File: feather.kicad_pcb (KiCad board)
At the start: 2 copper layers, 22.9 x 58.6 mm, 24 parts, among them J1 USB_C_Receptacle_USB2.0, J2 Conn_01x04_MountingPin, J3 Conn_ARM_SWD_TagConnect_TC203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, J4 2.54mm Header, J5 Micro_SD_Card_Det_Hirose_DM3AT, J6 2.54mm Header, SW1 BGS12P2L6, U1 TPS22917DBV, U10 TPS22917DBV, U2 nRF5340-CLXX, U3 nPM1100-CAXX, U4 TPS22917DBV, U5 USBLC6-2SC6, U6 TPS62173DSG, U7 MX25R3235FZNxx1, U8 nRF7002-QFXX, U9 TPS22917DBV

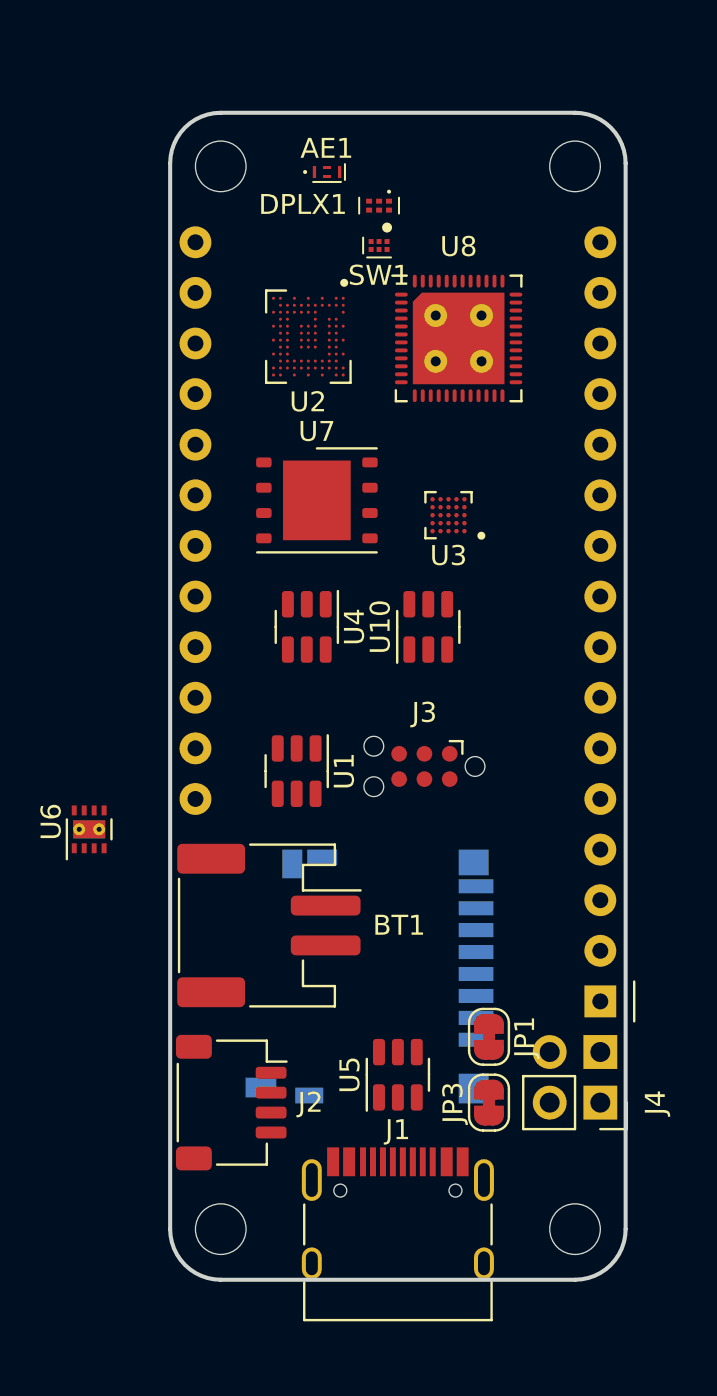
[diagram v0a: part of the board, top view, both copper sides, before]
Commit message: Added passvies and bus connections to nRF7002
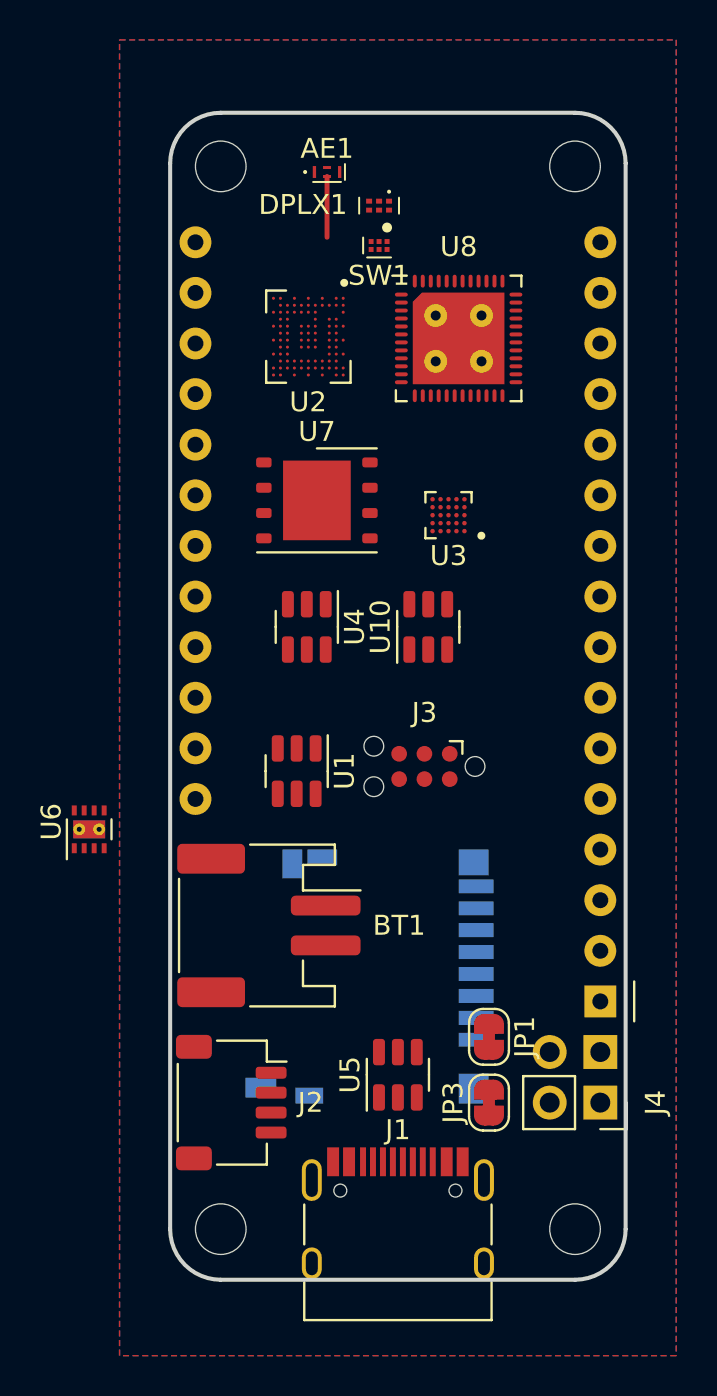
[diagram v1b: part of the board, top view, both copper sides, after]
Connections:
- A1 pad 26: unconnected-(A1-USB-Pad26) -> VBUS
- A1 pad 28: unconnected-(A1-VBAT-Pad28) -> /VBATT_
- U1 pad 1: unconnected-(U1-VIN-Pad1) -> VDD_nRF
- U1 pad 2: unconnected-(U1-GND-Pad2) -> GND
- U1 pad 3: unconnected-(U1-ON-Pad3) -> Net-(U1-ON)
- U1 pad 6: unconnected-(U1-VOUT-Pad6) -> Net-(U1-VOUT)
- U10 pad 1: unconnected-(U10-VIN-Pad1) -> +3.3V
- U10 pad 2: unconnected-(U10-GND-Pad2) -> GND
- U10 pad 3: unconnected-(U10-ON-Pad3) -> Net-(U10-ON)
- U10 pad 6: unconnected-(U10-VOUT-Pad6) -> Net-(U10-VOUT)
- U3 pad D1: /Connectivity/VBAT -> /VBATT_
- U3 pad D2: /Connectivity/VBAT -> /VBATT_
- U4 pad 1: unconnected-(U4-VIN-Pad1) -> +3.3V
- U4 pad 2: unconnected-(U4-GND-Pad2) -> GND
- U4 pad 3: unconnected-(U4-ON-Pad3) -> Net-(U4-ON)
- U4 pad 6: unconnected-(U4-VOUT-Pad6) -> Net-(J5-VDD)
- U7 pad 8: Net-(U7-VCC) -> Net-(U10-VOUT)
- U8 pad 13: /nRF7002/VBATT -> +3.3V
- U8 pad 20: /nRF7002/VBATT -> +3.3V
- U8 pad 31: /nRF7002/VBATT -> +3.3V
- U8 pad 48: unconnected-(U8-IOVDD-Pad48) -> Net-(U1-VOUT)
- U9 pad 1: unconnected-(U9-VIN-Pad1) -> VOUT
- U9 pad 2: unconnected-(U9-GND-Pad2) -> GND
- U9 pad 3: unconnected-(U9-ON-Pad3) -> /PowerSupply/BUCK_EN
- U9 pad 6: unconnected-(U9-VOUT-Pad6) -> Net-(U6-EN)
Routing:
- net Net-(AE1-FEED): track 0.00 -> 3.05 mm
- added copper zone on B.Cu, net GND
- added copper zone on F.Cu, net GND
- added copper zone on In1.Cu, net GND
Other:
- copper layers 2 -> 4

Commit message: Schematic complete.
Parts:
- removed JP2: 400mA Charge, Jumper:SolderJumper-2_P1.3mm_Open_RoundedPad1.0x1.5mm
- removed U1, U10, U9: TPS22917DBV, Package_TO_SOT_SMD:SOT-23-6
- removed U6: TPS62173DSG, Package_SON:WSON-8-1EP_2x2mm_P0.5mm_EP0.9x1.6mm_ThermalVias
- added C1: 10u, Capacitor_SMD:C_0402_1005Metric, F.Cu at (131.2, 59.1)
- added C10: 1u, Capacitor_SMD:C_0402_1005Metric, F.Cu at (205.5, 84.7)
- added C11: 1u, Capacitor_SMD:C_0402_1005Metric, F.Cu at (205.5, 86.6)
- added C12: 1u, Capacitor_SMD:C_0402_1005Metric, F.Cu at (205.5, 88.6)
- added C13: 100n, Capacitor_SMD:C_0201_0603Metric, F.Cu at (199.3, 83.7)
- added C14: 100n, Capacitor_SMD:C_0201_0603Metric, F.Cu at (199.3, 85.4)
- added C15: 100n, Capacitor_SMD:C_0201_0603Metric, F.Cu at (199.3, 87.2)
- added C16: 100n, Capacitor_SMD:C_0201_0603Metric, F.Cu at (199.3, 88.9)
- added C17: 100n, Capacitor_SMD:C_0201_0603Metric, F.Cu at (199.3, 90.7)
- added C18: 2.2n, Capacitor_SMD:C_0201_0603Metric, F.Cu at (95.7, 88.9)
- added C19: 1u, Capacitor_SMD:C_0402_1005Metric, F.Cu at (106.6, 89.1)
- added C2: 10u, Capacitor_SMD:C_0402_1005Metric, F.Cu at (131.2, 61.0)
- added C20: 4.7u, Capacitor_SMD:C_0402_1005Metric, F.Cu at (106.6, 91.0)
- added C21: 1u, Capacitor_SMD:C_0402_1005Metric, F.Cu at (106.6, 93.0)
- added C22: 100n, Capacitor_SMD:C_0201_0603Metric, F.Cu at (95.7, 90.7)
- added C24: C_Small, Capacitor_SMD:C_0201_0603Metric, F.Cu at (172.7, 106.6)
- added C25: C_Small, Capacitor_SMD:C_0201_0603Metric, F.Cu at (172.7, 109.0)
- added C28: 0.7p, Capacitor_SMD:C_0201_0603Metric, F.Cu at (180.3, 96.5)
- added C29: N.C., Capacitor_SMD:C_0201_0603Metric, F.Cu at (180.3, 98.8)
- added C3: 2.2u, Capacitor_SMD:C_0402_1005Metric, F.Cu at (131.2, 63.0)
- added C30: 12p, Capacitor_SMD:C_0201_0603Metric, F.Cu at (134.9, 79.2)
- added C31: 12p, Capacitor_SMD:C_0201_0603Metric, F.Cu at (134.9, 81.0)
- added C32: 4.7u, Capacitor_SMD:C_0402_1005Metric, F.Cu at (113.9, 78.1)
- added C33: 1u, Capacitor_SMD:C_0402_1005Metric, F.Cu at (93.5, 99.8)
- added C34: 2.2u, Capacitor_SMD:C_0402_1005Metric, F.Cu at (113.9, 80.1)
- added C35: 100n, Capacitor_SMD:C_0201_0603Metric, F.Cu at (111.2, 78.0)
- added C36: 4.7u, Capacitor_SMD:C_0402_1005Metric, F.Cu at (113.9, 82.0)
- added C37: 4.7u, Capacitor_SMD:C_0402_1005Metric, F.Cu at (113.9, 84.0)
- added C38: 1u, Capacitor_SMD:C_0402_1005Metric, F.Cu at (113.9, 86.0)
- added C39: 0.47u, Capacitor_SMD:C_0201_0603Metric, F.Cu at (111.2, 79.7)
- added C4: 1u, Capacitor_SMD:C_0402_1005Metric, F.Cu at (131.2, 65.0)
- added C40: 2.2u, Capacitor_SMD:C_0402_1005Metric, F.Cu at (116.8, 78.1)
- added C41: 0.22u, Capacitor_SMD:C_0201_0603Metric, F.Cu at (111.2, 81.5)
- added C42: 0.47u, Capacitor_SMD:C_0201_0603Metric, F.Cu at (111.2, 83.2)
- added C43: 22n, Capacitor_SMD:C_0201_0603Metric, F.Cu at (111.2, 85.0)
- added C44: 10n, Capacitor_SMD:C_0201_0603Metric, F.Cu at (111.2, 86.7)
- added C45: 1u, Capacitor_SMD:C_0402_1005Metric, F.Cu at (116.8, 80.1)
- added C46: 1u, Capacitor_SMD:C_0402_1005Metric, F.Cu at (116.8, 82.0)
- added C47: 100n, Capacitor_SMD:C_0201_0603Metric, F.Cu at (111.2, 88.5)
- added C48: 2.2u, Capacitor_SMD:C_0402_1005Metric, F.Cu at (116.8, 84.0)
- added C5: 10u, Capacitor_SMD:C_0402_1005Metric, F.Cu at (98.4, 99.8)
- added C50: 4.7u, Capacitor_SMD:C_0402_1005Metric, F.Cu at (116.8, 86.0)
- added C53: 8p, Capacitor_SMD:C_0201_0603Metric, F.Cu at (144.4, 62.4)
- added C54: 8p, Capacitor_SMD:C_0201_0603Metric, F.Cu at (146.9, 58.9)
- added C55: 8p, Capacitor_SMD:C_0201_0603Metric, F.Cu at (178.2, 86.8)
- added C56: 8p, Capacitor_SMD:C_0201_0603Metric, F.Cu at (183.2, 86.8)
- added C57: 10u, Capacitor_SMD:C_0402_1005Metric, F.Cu at (131.2, 68.9)
- added C58: 100n, Capacitor_SMD:C_0402_1005Metric, F.Cu at (131.2, 70.9)
- added C59: 1u, Capacitor_SMD:C_0402_1005Metric, F.Cu at (131.2, 72.8)
- added C6: 1u, Capacitor_SMD:C_0402_1005Metric, F.Cu at (100.8, 89.1)
- added C7: 10u, Capacitor_SMD:C_0402_1005Metric, F.Cu at (131.2, 66.9)
- added C8: 4.7u, Capacitor_SMD:C_0402_1005Metric, F.Cu at (100.8, 91.0)
- added C9: 1u, Capacitor_SMD:C_0402_1005Metric, F.Cu at (183.4, 90.0)
- added D1: LED_ARGB, LED_SMD:LED_SK6812_EC15_1.5x1.5mm, F.Cu at (134.2, 70.1)
- added D3: LED_Small, LED_SMD:LED_0805_2012Metric, F.Cu at (155.5, 58.4)
- added F1: 1A PTC, Fuse:Fuse_0402_1005Metric, F.Cu at (173.4, 64.8)
- added F2: 1A PTC, Fuse:Fuse_0402_1005Metric, F.Cu at (111.5, 97.4)
- added FB1: FerriteBead_Small, Inductor_SMD:L_0402_1005Metric, F.Cu at (172.3, 64.9)
- added L1: 2.2u, Inductor_SMD:L_0805_2012Metric, F.Cu at (175.2, 80.6)
- added L2: 10u, Inductor_SMD:L_0603_1608Metric, F.Cu at (141.2, 59.3)
- added L3: 10u, Inductor_SMD:L_0603_1608Metric, F.Cu at (141.2, 61.8)
- added L5: 3.3u, Inductor_SMD:L_0201_0603Metric, F.Cu at (173.1, 107.8)
- added L6: 2.2u, Inductor_SMD:L_0805_2012Metric, F.Cu at (134.9, 62.2)
- added L7: 2.2n, Inductor_SMD:L_0201_0603Metric, F.Cu at (180.0, 95.3)
- added L8: 2.2n, Inductor_SMD:L_0201_0603Metric, F.Cu at (180.0, 97.6)
- added L9: 3.3u, Inductor_SMD:L_0603_1608Metric, F.Cu at (131.8, 77.1)
- added Q2: Q_PMOS_GSD, Package_TO_SOT_SMD:SOT-323_SC-70, F.Cu at (175.2, 74.4)
- added R1: 47k, Resistor_SMD:R_0603_1608Metric, F.Cu at (134.7, 64.8)
- added R10: 100k, Resistor_SMD:R_0603_1608Metric, B.Cu at (172.0, 86.1)
- added R13: 33, Resistor_SMD:R_0603_1608Metric, B.Cu at (173.3, 79.5)
- added R2: 360k, Resistor_SMD:R_0603_1608Metric, F.Cu at (134.7, 67.3)
- added R3: 5.1k, Resistor_SMD:R_0603_1608Metric, F.Cu at (141.2, 64.3)
- added R4: 5.1k, Resistor_SMD:R_0603_1608Metric, F.Cu at (141.2, 66.9)
- added R5: 5.1k, Resistor_SMD:R_0603_1608Metric, F.Cu at (152.2, 69.1)
- added R6: 5.1k, Resistor_SMD:R_0603_1608Metric, F.Cu at (152.2, 71.6)
- added R8: 470, Resistor_SMD:R_0805_2012Metric, F.Cu at (155.5, 54.0)
- added Y1: 40MHz, Crystal:Crystal_SMD_2016-4Pin_2.0x1.6mm, F.Cu at (177.5, 100.5)
- added Y2: 32MHz, Crystal:Crystal_SMD_2016-4Pin_2.0x1.6mm, F.Cu at (176.9, 93.9)
- added Y3: 32.768KHz, Crystal:Crystal_SMD_3215-2Pin_3.2x1.5mm, F.Cu at (180.7, 87.3)
- AE1: value ~ -> Capacitor_SMD:C_0402_1005Metric
- DPLX1: value 2450DP14A6000 -> DPX105950DT-6112A2; footprint rf-lib:2450DP14A6000 -> rf-lib:DPX105950DT-6112A2
- J3, U4, U7: moved to B.Cu
- U3: value nPM1100-CAXX -> nPM1300-QEXX; footprint nordic-lib-kicad-npm:BGA-25_5x5_2.075x2.075mm -> Package_DFN_QFN:QFN-32-1EP_5x5mm_P0.5mm_EP3.6x3.6mm_ThermalVias
- moved AE1 58.8 mm to (173.1, 113.5), turned to 180 degrees
- moved A1 58.4 mm to (184.7, 111.5), turned to 180 degrees
- moved J1 51.0 mm to (175.8, 57.8), turned to 180 degrees
- moved DPLX1 49.2 mm to (173.0, 105.4), turned to -45 degrees
- moved SW1 46.5 mm to (175.2, 104.9)
- moved JP3 44.8 mm to (165.5, 61.2), turned to -90 degrees
- moved J4 44.7 mm to (165.6, 64.5), turned to 90 degrees
- moved JP1 40.7 mm to (168.1, 61.2)
- moved J3 40.4 mm to (141.6, 89.9), turned to 90 degrees
- moved J6 39.1 mm to (168.1, 67.0)
- moved J2 39.0 mm to (184.1, 64.5), turned to 90 degrees
- moved U8 38.0 mm to (172.3, 99.6), turned to 90 degrees
- moved U5 34.6 mm to (175.8, 65.9), turned to -90 degrees
- moved U2 29.4 mm to (180.7, 92.1), turned to 90 degrees
- moved J5 24.5 mm to (177.2, 70.8), turned to 90 degrees
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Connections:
- net Net-(U8-OTPVDD) renamed /nRF7002/PWRIOVDD
- A1 pad 1: unconnected-(A1-~{RESET}-Pad1) -> /~{RESET}
- A1 pad 10: unconnected-(A1-A5-Pad10) -> /AIN5
- A1 pad 11: unconnected-(A1-SCK-Pad11) -> /OUT_SPI0
- A1 pad 12: unconnected-(A1-MOSI-Pad12) -> /OUT_SPI1
- A1 pad 13: unconnected-(A1-MISO-Pad13) -> /OUT_SPI2
- A1 pad 14: unconnected-(A1-RX-Pad14) -> /OUT_UART0
- A1 pad 15: unconnected-(A1-TX-Pad15) -> /OUT_UART1
- A1 pad 16: unconnected-(A1-SPARE-Pad16) -> /OUT7
- A1 pad 17: unconnected-(A1-SDA-Pad17) -> /OUT_TWI0
- A1 pad 18: unconnected-(A1-SCL-Pad18) -> /OUT_TWI1
- A1 pad 19: unconnected-(A1-D0-Pad19) -> /OUT0
- A1 pad 2: +3.3V -> +3V3
- A1 pad 20: unconnected-(A1-D1-Pad20) -> /OUT1
- A1 pad 21: unconnected-(A1-D2-Pad21) -> /OUT2
- A1 pad 22: unconnected-(A1-D3-Pad22) -> /OUT3
- A1 pad 23: unconnected-(A1-D4-Pad23) -> /OUT4
- A1 pad 24: unconnected-(A1-D5-Pad24) -> /OUT5
- A1 pad 25: unconnected-(A1-D6-Pad25) -> /OUT6
- A1 pad 26: VBUS -> /VBUS_
- A1 pad 27: unconnected-(A1-EN-Pad27) -> /REG_EN
- A1 pad 5: unconnected-(A1-A0-Pad5) -> /AIN0
- A1 pad 6: unconnected-(A1-A1-Pad6) -> /AIN1
- A1 pad 7: unconnected-(A1-A2-Pad7) -> /AIN2
- A1 pad 8: unconnected-(A1-A3-Pad8) -> /AIN3
- A1 pad 9: unconnected-(A1-A4-Pad9) -> /AIN4
- DPLX1 pad 3: GND -> Net-(DPLX1-LOWFREQ)
- J1 pad A5: Net-(J1-CC1) -> /Connectivity/CC1
- J1 pad B5: Net-(J1-CC2) -> /Connectivity/CC2
- J2 pad 3: /Connectivity/SDA_ -> /OUT_TWI0
- J2 pad 4: /Connectivity/SCL_ -> /OUT_TWI1
- J3 pad 3: /Connectivity/~{SOC_RESET} -> /~{RESET}
- J3 pad 6: /Connectivity/SOC_SWO -> unconnected-(J3-SWO-Pad6)
- J5 pad 10: unconnected-(J5-DET_A-Pad10) -> /NonvolatileMemory/SD_INSERTED
- J5 pad 2: unconnected-(J5-DAT3/CD-Pad2) -> /NonvolatileMemory/FLASH_SD_CTRL4
- J5 pad 3: unconnected-(J5-CMD-Pad3) -> /NonvolatileMemory/FLASH_SD_CTRL2
- J5 pad 5: unconnected-(J5-CLK-Pad5) -> /NonvolatileMemory/FLASH_SD_CTRL1
- J5 pad 7: unconnected-(J5-DAT0-Pad7) -> /NonvolatileMemory/FLASH_SD_CTRL3
- J5 pad 9: unconnected-(J5-DET_B-Pad9) -> GND
- J6 pad 2: VBUS -> /VBUS_
- JP3 pad 2: VBUS -> /VBUS_
- SW1 pad 1: /nRF5340/NRF7002_2G4 -> /nRF5340/NRF5340_2G4
- SW1 pad 3: /nRF5340/NRF5340_2G4 -> /nRF5340/NRF7002_2G4
- SW1 pad 4: VDD_nRF -> +3V3
- SW1 pad 6: unconnected-(SW1-CTRL-Pad6) -> /nRF5340/ANT_CTRL
- U2 pad A1: unconnected-(U2A-XC1-PadA1) -> Net-(U2A-XC1)
- U2 pad A2: unconnected-(U2A-XC2-PadA2) -> Net-(U2A-XC2)
- U2 pad A3: VDD_nRF -> +3V3
- U2 pad B10: VDD_nRF -> +3V3
- U2 pad B12: VOUT -> +3V3
- U2 pad B7: VDD_nRF -> +3V3
- U2 pad C10: unconnected-(U2A-P1.15-PadC10) -> /nRF5340/ANT_CTRL
- U2 pad C4: unconnected-(U2A-P0.30-PadC4) -> /OUT0
- U2 pad C5: unconnected-(U2A-P0.31-PadC5) -> /OUT1
- U2 pad C6: unconnected-(U2A-P1.11-PadC6) -> /nRF5340/NRF7002_CTRL3
- U2 pad C7: unconnected-(U2A-P1.12-PadC7) -> /nRF5340/NRF7002_CTRL4
- U2 pad C8: unconnected-(U2A-P1.13-PadC8) -> /nRF5340/NRF7002_CTRL5
- U2 pad C9: unconnected-(U2A-P1.14-PadC9) -> /nRF5340/NRF7002_CTRL6
- U2 pad D10: unconnected-(U2A-P1.00-PadD10) -> /OUT2
- U2 pad D11: Net-(U2B-DCCH) -> unconnected-(U2B-DCCH-PadD11)
- U2 pad D2: VDD_nRF -> +3V3
- U2 pad E10: unconnected-(U2A-P1.01-PadE10) -> /OUT3
- U2 pad E11: VDD_nRF -> +3V3
- U2 pad E2: unconnected-(U2A-P0.29-PadE2) -> /OUT_UART1
- U2 pad E3: unconnected-(U2A-P0.28/AIN7-PadE3) -> /NonvolatileMemory/SD_INSERTED
- U2 pad E4: unconnected-(U2A-P1.10-PadE4) -> /nRF5340/NRF7002_CTRL2
- U2 pad F1: /nRF5340/SWDIO_ -> /Connectivity/SOC_SWDIO
- U2 pad F10: unconnected-(U2A-P0.05/AIN1-PadF10) -> /AIN1
- U2 pad F11: unconnected-(U2A-P0.00/XL1-PadF11) -> Net-(U2A-P0.00/XL1)
- U2 pad F12: unconnected-(U2A-P0.01/XL2-PadF12) -> Net-(U2A-P0.01/XL2)
- U2 pad F2: /nRF5340/SWCLK_ -> /Connectivity/SOC_SWCLK
- U2 pad F3: unconnected-(U2A-P1.08-PadF3) -> /nRF5340/NRF7002_CTRL0
- U2 pad G10: unconnected-(U2A-P0.04/AIN0-PadG10) -> /AIN0
- U2 pad G2: /nRF5340/~{RESET}_ -> /~{RESET}
- U2 pad G3: unconnected-(U2A-P1.07-PadG3) -> /OUT7
- U2 pad H1: unconnected-(U2A-P0.27/AIN6-PadH1) -> /NonvolatileMemory/SD_CARD_EN
- U2 pad H10: unconnected-(U2A-P0.06/AIN2-PadH10) -> /AIN2
- U2 pad H11: VDD_nRF -> +3V3
- U2 pad H2: unconnected-(U2A-P1.09-PadH2) -> /nRF5340/NRF7002_CTRL1
- U2 pad H3: unconnected-(U2A-P0.23-PadH3) -> /PowerSupply/NPM_SDA
- U2 pad J10: unconnected-(U2A-P0.07/AIN3-PadJ10) -> /AIN3
- U2 pad J11: unconnected-(U2A-P1.02/TWI-PadJ11) -> /OUT_TWI0
- U2 pad J2: unconnected-(U2A-P0.26/AIN5-PadJ2) -> /AIN5
- U2 pad J3: unconnected-(U2A-P1.06-PadJ3) -> /OUT6
- U2 pad J4: unconnected-(U2A-P0.21-PadJ4) -> /OUT_SPI2
- U2 pad J5: unconnected-(U2A-P0.19-PadJ5) -> /OUT_SPI0
- U2 pad J6: unconnected-(U2A-P0.12/TRACECLK/DCX-PadJ6) -> /NonvolatileMemory/FLASH_SD_CTRL4
- U2 pad J7: unconnected-(U2A-P0.11/TRACEDATA0/~{CS}-PadJ7) -> /NonvolatileMemory/FLASH_SD_CTRL0
- U2 pad J8: unconnected-(U2A-P0.10/TRACEDATA1/MISO-PadJ8) -> /NonvolatileMemory/FLASH_SD_CTRL3
- U2 pad J9: unconnected-(U2A-P0.09/TRACEDATA2/MOSI-PadJ9) -> /NonvolatileMemory/FLASH_SD_CTRL2
- U2 pad K1: VDD_nRF -> +3V3
- U2 pad K12: unconnected-(U2A-P1.03/TWI-PadK12) -> /OUT_TWI1
- U2 pad K2: unconnected-(U2A-P0.24-PadK2) -> /OUT_UART0
- U2 pad K3: unconnected-(U2A-P1.04-PadK3) -> /OUT4
- U2 pad K4: unconnected-(U2A-P0.22-PadK4) -> /PowerSupply/NPM_SCL
- U2 pad K5: unconnected-(U2A-P0.20-PadK5) -> /OUT_SPI1
- U2 pad L1: unconnected-(U2A-P0.25/AIN4-PadL1) -> /AIN4
- U2 pad L11: VDD_nRF -> +3V3
- U2 pad L12: unconnected-(U2A-P0.08/TRACEDATA3/SCK-PadL12) -> /NonvolatileMemory/FLASH_SD_CTRL1
- U2 pad L3: unconnected-(U2A-P1.05-PadL3) -> /OUT5
- U2 pad L5: VDD_nRF -> +3V3
- U4 pad 3: Net-(U4-ON) -> /NonvolatileMemory/SD_CARD_EN
- U4 pad 6: Net-(J5-VDD) -> Net-(U4-VOUT)
- U5 pad 1: /Connectivity/D- -> /Connectivity/D+
- U5 pad 3: /Connectivity/D+ -> /Connectivity/D-
- U5 pad 4: /Connectivity/D+ -> /Connectivity/D-
- U5 pad 5: VBUS -> /VBUS_
- U5 pad 6: /Connectivity/D- -> /Connectivity/D+
- U7 pad 1: unconnected-(U7-~{CS}-Pad1) -> /NonvolatileMemory/FLASH_SD_CTRL0
- U7 pad 2: unconnected-(U7-SO/SIO1-Pad2) -> /NonvolatileMemory/FLASH_SD_CTRL3
- U7 pad 5: unconnected-(U7-SI/SIO0-Pad5) -> /NonvolatileMemory/FLASH_SD_CTRL2
- U7 pad 6: unconnected-(U7-SCLK-Pad6) -> /NonvolatileMemory/FLASH_SD_CTRL1
- U7 pad 8: Net-(U10-VOUT) -> /FLASH_VDD
- U8 pad 11: unconnected-(U8-SXLDO-Pad11) -> Net-(U8-SXLDO)
- U8 pad 13: +3.3V -> +3V3
- U8 pad 14: unconnected-(U8-RFVDD-Pad14) -> Net-(U8-RFVDD)
- U8 pad 16: unconnected-(U8-XOLDO-Pad16) -> Net-(U8-XOLDO)
- U8 pad 19: unconnected-(U8-AFELDO-Pad19) -> Net-(U8-AFELDO)
- U8 pad 20: +3.3V -> +3V3
- U8 pad 25: unconnected-(U8-BUCKVBAT-Pad25) -> +3V3
- U8 pad 29: unconnected-(U8-BUCKVMID-Pad29) -> Net-(U8-BUCKVMID)
- U8 pad 30: unconnected-(U8-BUCKEN-Pad30) -> /nRF5340/NRF7002_CTRL0
- U8 pad 31: +3.3V -> +3V3
- U8 pad 33: unconnected-(U8-DIGVDD-Pad33) -> Net-(U8-DIGVDD)
- U8 pad 41: unconnected-(U8-COEX_STATUS0-Pad41) -> /nRF5340/NRF7002_CTRL1
- U8 pad 42: unconnected-(U8-COEX_REQ-Pad42) -> /nRF5340/NRF7002_CTRL2
- U8 pad 43: unconnected-(U8-COEX_GRANT-Pad43) -> /nRF5340/NRF7002_CTRL3
- U8 pad 44: unconnected-(U8-SW_CTRL0-Pad44) -> /nRF5340/NRF7002_CTRL5
- U8 pad 45: unconnected-(U8-SW_CTRL1-Pad45) -> /nRF5340/NRF7002_CTRL6
- U8 pad 46: unconnected-(U8-HOST_IRQ-Pad46) -> /nRF5340/NRF7002_CTRL4
- U8 pad 48: Net-(U1-VOUT) -> /NRF7002_IOVDD
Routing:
- net Net-(AE1-FEED): track 3.05 -> 0.00 mm
- added copper zone on In1.Cu, net +3V3
